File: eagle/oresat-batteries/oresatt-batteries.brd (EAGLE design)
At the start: 160 x 100 mm, 4 parts

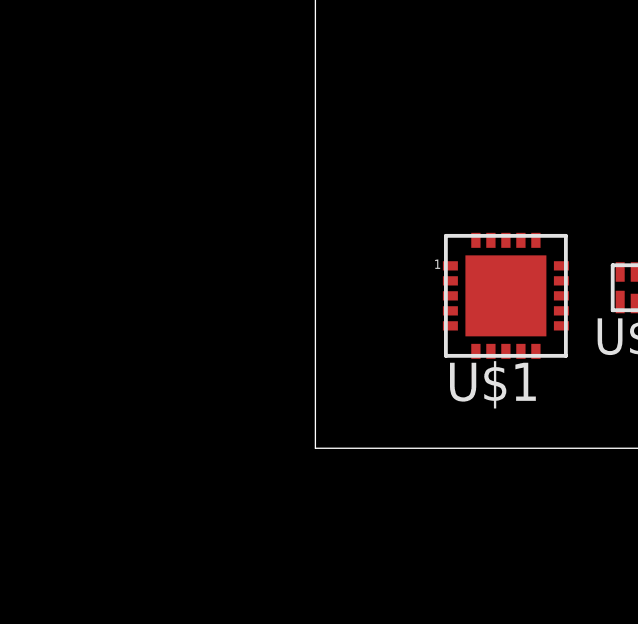
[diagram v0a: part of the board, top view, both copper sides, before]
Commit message: Added crystal, CAN transciever
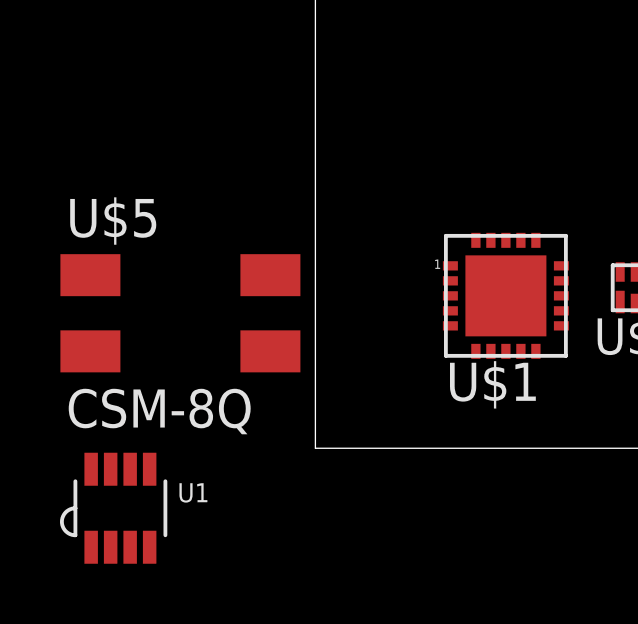
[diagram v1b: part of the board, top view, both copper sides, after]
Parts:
- added U$5: CSM-8Q, oresat-batteries:4-SMD
- added U1: TCAN330, oresat-batteries:SOT23-8_TI-DCN
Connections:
- new net GND: U1.2
- new net VCC: U1.3
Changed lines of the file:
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@@
 <element name="U$3" library="oresat-batteries" package="WDFN8_3X4" value="LC709203F" x="15.24" y="5.08"/>
 <element name="U$4" library="oresat-batteries" package="UFQFPN-28" value="STM32F042G" x="21" y="11"/>
+<element name="U$5" library="oresat-batteries" package="4-SMD" value="CSM-8Q" x="-4.5" y="4.5"/>
+<element name="U1" library="oresat-batteries" package="SOT23-8_TI-DCN" value="TCAN330" x="-6.5" y="-2"/>
 </elements>
 <signals>
@@
 <contactref element="U$4" pad="18"/>
 </signal>
+<signal name="GND">
+<contactref element="U1" pad="2"/>
+</signal>
+<signal name="VCC">
+<contactref element="U1" pad="3"/>
+</signal>
 </signals>

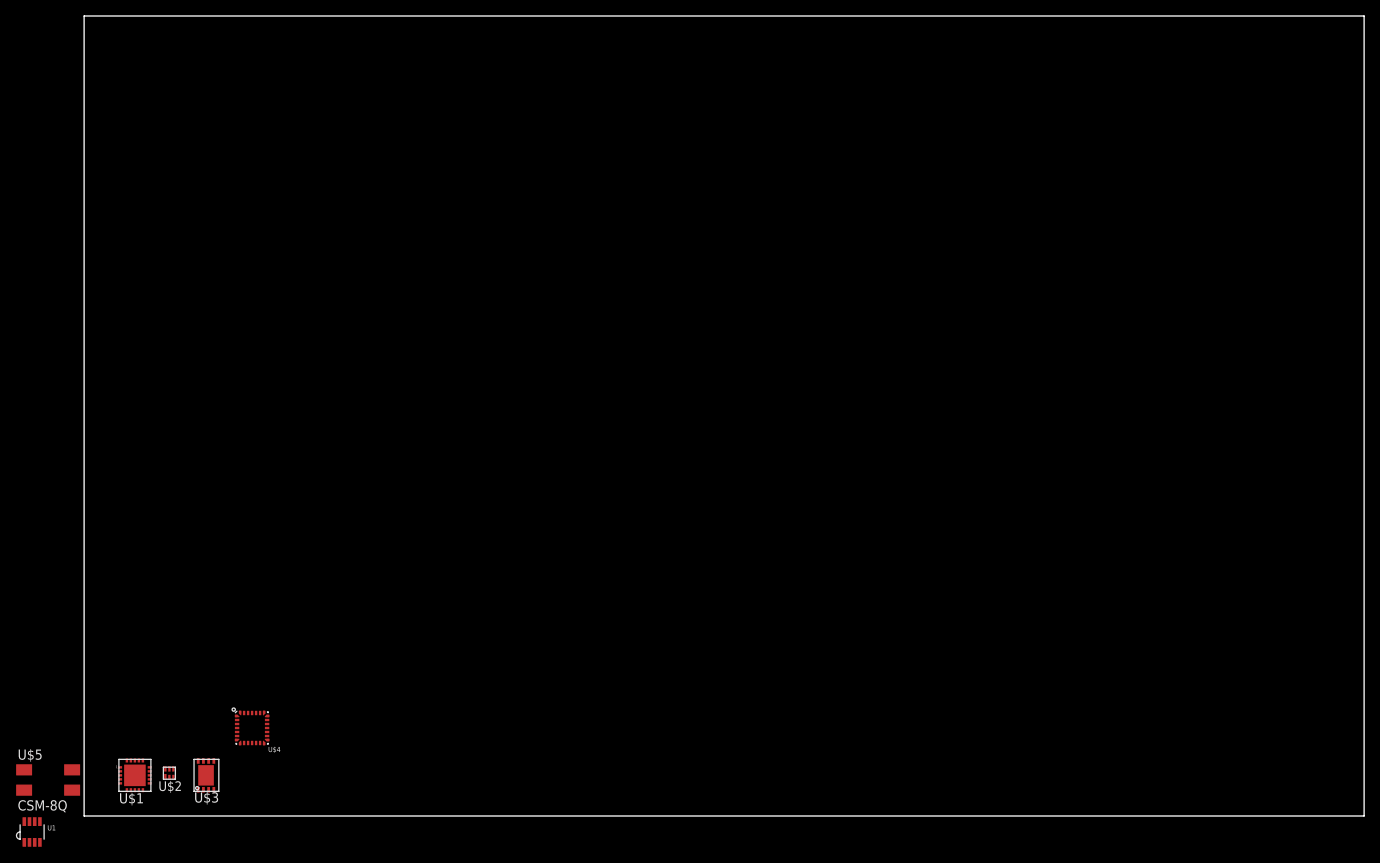
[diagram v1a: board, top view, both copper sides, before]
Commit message: Changed board to real max dimensions.  Added 40pin connector
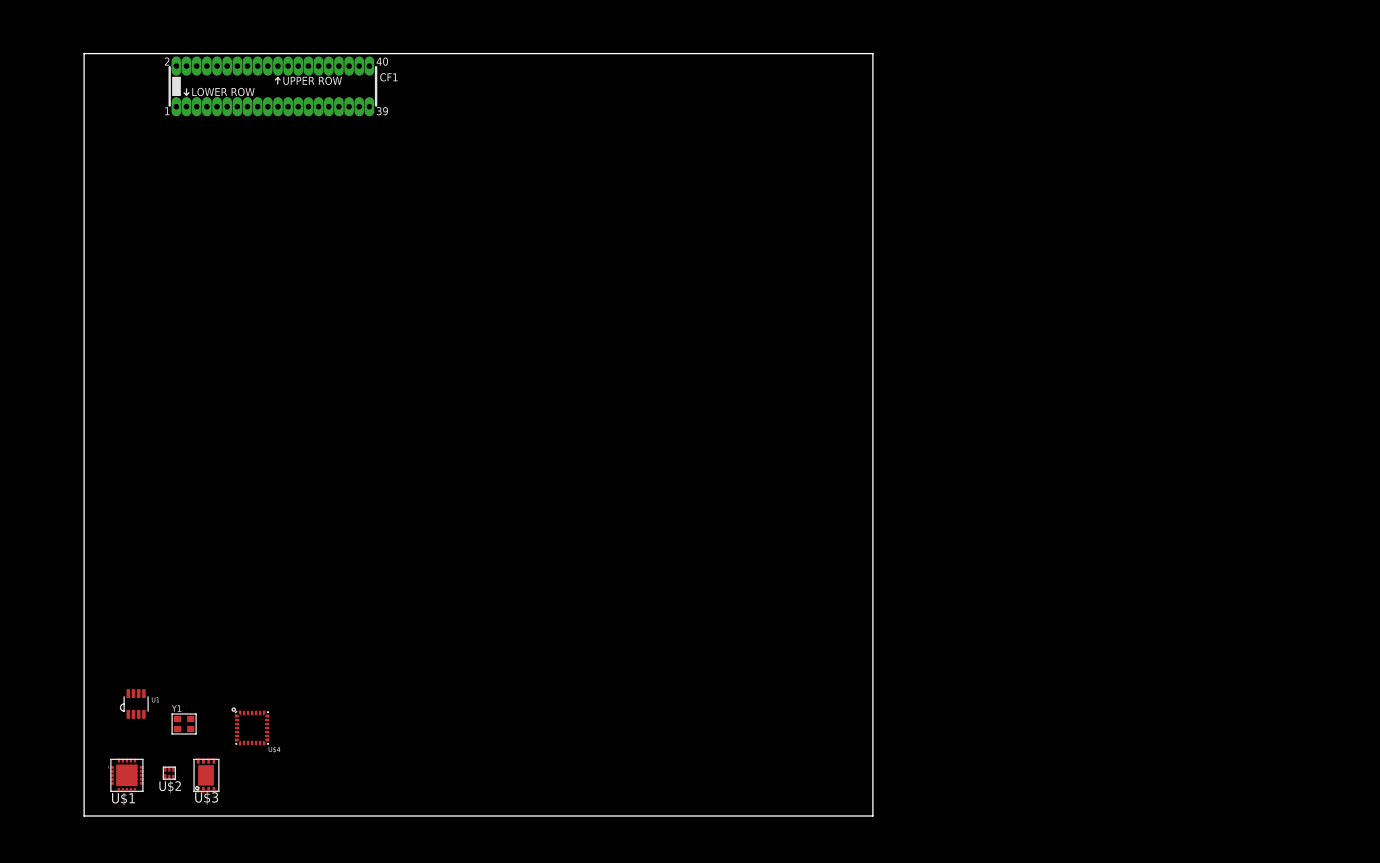
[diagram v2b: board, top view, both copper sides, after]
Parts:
- removed U$5: CSM-8Q, oresat-batteries:4-SMD
- added CF1: ORESAT-CONNECTOR-40PIN, low-gain-radio:HARWIN-ARCHER-M50-3202045
- added Y1: (no value), low-gain-radio:CRYSTAL_2.5X2
- moved U1 20.6 mm to (6.50, 14.0)
- moved U$1 1.00 mm to (5.35, 5.08)
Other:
- board size 160 x 100 mm -> 98.6 x 95.3 mm
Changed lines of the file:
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@@
 <setting verticaltext="up"/>
 </settings>
-<grid distance="0.5" unitdist="mm" unit="mm" style="lines" multiple="1" display="yes" altdistance="0.025" altunitdist="inch" altunit="inch"/>
+<grid distance="0.1" unitdist="mm" unit="mm" style="lines" multiple="1" display="yes" altdistance="0.025" altunitdist="inch" altunit="inch"/>
 <layers>
 <layer number="1" name="Top" color="4" fill="1" visible="yes" active="yes"/>
@@
 <layer number="48" name="Document" color="7" fill="1" visible="yes" active="yes"/>
 <layer number="49" name="Reference" color="7" fill="1" visible="yes" active="yes"/>
+<layer number="50" name="dxf" color="7" fill="1" visible="yes" active="yes"/>
 <layer number="51" name="tDocu" color="7" fill="1" visible="yes" active="yes"/>
 <layer number="52" name="bDocu" color="7" fill="1" visible="yes" active="yes"/>
+<layer number="53" name="tGND_GNDA" color="7" fill="1" visible="yes" active="yes"/>
+<layer number="54" name="bGND_GNDA" color="7" fill="1" visible="yes" active="yes"/>
+<layer number="56" name="wert" color="7" fill="1" visible="yes" active="yes"/>
+<layer number="57" name="tCAD" color="7" fill="1" visible="yes" active="yes"/>
+<layer number="58" name="b3D" color="7" fill="1" visible="yes" active="yes"/>
+<layer number="59" name="Invisible" color="7" fill="1" visible="yes" active="yes"/>
+<layer number="61" name="stand" color="7" fill="1" visible="yes" active="yes"/>
 <layer number="90" name="Modules" color="5" fill="1" visible="no" active="no"/>
 <layer number="91" name="Nets" color="2" fill="1" visible="no" active="no"/>
@@
 <layer number="97" name="Info" color="7" fill="1" visible="no" active="no"/>
 <layer number="98" name="Guide" color="6" fill="1" visible="no" active="no"/>
+<layer number="99" name="SpiceOrder" color="7" fill="1" visible="no" active="no"/>
+<layer number="100" name="TODO" color="7" fill="1" visible="yes" active="yes"/>
+<layer number="101" name="Hidden" color="7" fill="1" visible="yes" active="yes"/>
+<layer number="102" name="Changes" color="7" fill="1" visible="yes" active="yes"/>
+<layer number="103" name="tMap" color="7" fill="1" visible="yes" active="yes"/>
+<layer number="104" name="Name" color="7" fill="1" visible="yes" active="yes"/>
+<layer number="105" name="Beschreib" color="7" fill="1" visible="yes" active="yes"/>
+<layer number="106" name="BGA-Top" color="7" fill="1" visible="yes" active="yes"/>
+<layer number="107" name="BD-Top" color="7" fill="1" visible="yes" active="yes"/>
+<layer number="108" name="tplace-old" color="7" fill="1" visible="yes" active="yes"/>
+<layer number="109" name="ref-old" color="7" fill="1" visible="yes" active="yes"/>
+<layer number="110" name="fp0" color="7" fill="1" visible="yes" active="yes"/>
+<layer number="111" name="LPC17xx" color="7" fill="1" visible="yes" active="yes"/>
+<layer number="112" name="tSilk" color="7" fill="1" visible="yes" active="yes"/>
+<layer number="113" name="ReferenceLS" color="7" fill="1" visible="yes" active="yes"/>
+<layer number="114" name="secv1" color="7" fill="1" visible="yes" active="yes"/>
+<layer number="115" name="secv12" color="7" fill="1" visible="yes" active="yes"/>
+<layer number="116" name="Patch_BOT" color="7" fill="1" visible="yes" active="yes"/>
+<layer number="117" name="secv21" color="7" fill="1" visible="yes" active="yes"/>
+<layer number="118" name="Rect_Pads" color="7" fill="1" visible="yes" active="yes"/>
+<layer number="121" name="_tsilk" color="7" fill="1" visible="yes" active="yes"/>
+<layer number="122" name="_bsilk" color="7" fill="1" visible="yes" active="yes"/>
+<layer number="123" name="tTestmark" color="7" fill="1" visible="yes" active="yes"/>
+<layer number="124" name="bTestmark" color="7" fill="1" visible="yes" active="yes"/>
+<layer number="125" name="_tNames" color="7" fill="1" visible="yes" active="yes"/>
+<layer number="126" name="_bNames" color="7" fill="1" visible="yes" active="yes"/>
+<layer number="127" name="_tValues" color="7" fill="1" visible="yes" active="yes"/>
+<layer number="128" name="_bValues" color="7" fill="1" visible="yes" active="yes"/>
+<layer number="130" name="bLogo" color="7" fill="1" visible="yes" active="yes"/>
+<layer number="131" name="tAdjust" color="7" fill="1" visible="yes" active="yes"/>
+<layer number="132" name="bAdjust" color="7" fill="1" visible="yes" active="yes"/>
+<layer number="144" name="Drill_legend" color="7" fill="1" visible="yes" active="yes"/>
+<layer number="150" name="Notes" color="7" fill="1" visible="yes" active="yes"/>
+<layer number="151" name="HeatSink" color="7" fill="1" visible="yes" active="yes"/>
+<layer number="152" name="_bDocu" color="7" fill="1" visible="yes" active="yes"/>
+<layer number="153" name="FabDoc1" color="7" fill="1" visible="yes" active="yes"/>
+<layer number="154" name="FabDoc2" color="7" fill="1" visible="yes" active="yes"/>
+<layer number="155" name="FabDoc3" color="7" fill="1" visible="yes" active="yes"/>
+<layer number="199" name="Contour" color="7" fill="1" visible="yes" active="yes"/>
+<layer number="200" name="200bmp" color="7" fill="1" visible="yes" active="yes"/>
+<layer number="201" name="201bmp" color="7" fill="1" visible="yes" active="yes"/>
+<layer number="202" name="202bmp" color="7" fill="1" visible="yes" active="yes"/>
+<layer number="203" name="203bmp" color="7" fill="1" visible="yes" active="yes"/>
+<layer number="204" name="204bmp" color="7" fill="1" visible="yes" active="yes"/>
+<layer number="205" name="205bmp" color="7" fill="1" visible="yes" active="yes"/>
+<layer number="206" name="206bmp" color="7" fill="1" visible="yes" active="yes"/>
+<layer number="207" name="207bmp" color="7" fill="1" visible="yes" active="yes"/>
+<layer number="208" name="208bmp" color="7" fill="1" visible="yes" active="yes"/>
+<layer number="209" name="209bmp" color="7" fill="1" visible="yes" active="yes"/>
+<layer number="210" name="210bmp" color="7" fill="1" visible="yes" active="yes"/>
+<layer number="211" name="211bmp" color="7" fill="1" visible="yes" active="yes"/>
+<layer number="212" name="212bmp" color="7" fill="1" visible="yes" active="yes"/>
+<layer number="213" name="213bmp" color="7" fill="1" visible="yes" active="yes"/>
+<layer number="214" name="214bmp" color="7" fill="1" visible="yes" active="yes"/>
+<layer number="215" name="215bmp" color="7" fill="1" visible="yes" active="yes"/>
+<layer number="216" name="216bmp" color="7" fill="1" visible="yes" active="yes"/>
+<layer number="217" name="217bmp" color="7" fill="1" visible="yes" active="yes"/>
+<layer number="218" name="218bmp" color="7" fill="1" visible="yes" active="yes"/>
+<layer number="219" name="219bmp" color="7" fill="1" visible="yes" active="yes"/>
+<layer number="220" name="220bmp" color="7" fill="1" visible="yes" active="yes"/>
+<layer number="221" name="221bmp" color="7" fill="1" visible="yes" active="yes"/>
+<layer number="222" name="222bmp" color="7" fill="1" visible="yes" active="yes"/>
+<layer number="223" name="223bmp" color="7" fill="1" visible="yes" active="yes"/>
+<layer number="224" name="224bmp" color="7" fill="1" visible="yes" active="yes"/>
+<layer number="225" name="225bmp" color="7" fill="1" visible="yes" active="yes"/>
+<layer number="226" name="226bmp" color="7" fill="1" visible="yes" active="yes"/>
+<layer number="227" name="227bmp" color="7" fill="1" visible="yes" active="yes"/>
+<layer number="228" name="228bmp" color="7" fill="1" visible="yes" active="yes"/>
+<layer number="231" name="Eagle3D_PG1" color="7" fill="1" visible="yes" active="yes"/>
+<layer number="232" name="Eagle3D_PG2" color="7" fill="1" visible="yes" active="yes"/>
+<layer number="233" name="Eagle3D_PG3" color="7" fill="1" visible="yes" active="yes"/>
+<layer number="248" name="Housing" color="7" fill="1" visible="yes" active="yes"/>
+<layer number="249" name="Edge" color="7" fill="1" visible="yes" active="yes"/>
+<layer number="250" name="Descript" color="7" fill="1" visible="yes" active="yes"/>
+<layer number="251" name="SMDround" color="7" fill="1" visible="yes" active="yes"/>
+<layer number="254" name="cooling" color="7" fill="1" visible="yes" active="yes"/>
 </layers>
 <board>
 <plain>
-<wire x1="0" y1="0" x2="160" y2="0" width="0" layer="20"/>
-<wire x1="160" y1="0" x2="160" y2="100" width="0" layer="20"/>
-<wire x1="160" y1="100" x2="0" y2="100" width="0" layer="20"/>
-<wire x1="0" y1="100" x2="0" y2="0" width="0" layer="20"/>
+<wire x1="0" y1="0" x2="98.6" y2="0" width="0" layer="20"/>
+<wire x1="98.6" y1="0" x2="98.6" y2="95.3" width="0" layer="20"/>
+<wire x1="98.6" y1="95.3" x2="0" y2="95.3" width="0" layer="20"/>
+<wire x1="0" y1="95.3" x2="0" y2="0" width="0" layer="20"/>
 </plain>
 <attributes>
@@
 </autorouter>
 <elements>
-<element name="U$1" library="oresat-batteries" package="20_4X4_VVTQ" value="ADP5063" x="6.35" y="5.08"/>
+<element name="U$1" library="oresat-batteries" package="20_4X4_VVTQ" value="ADP5063" x="5.35" y="5.08"/>
 <element name="U$2" library="oresat-batteries" package="PSOP6" value="BQ2970" x="10.66" y="5.35"/>
 <element name="U$3" library="oresat-batteries" package="WDFN8_3X4" value="LC709203F" x="15.24" y="5.08"/>
 <element name="U$4" library="oresat-batteries" package="UFQFPN-28" value="STM32F042G" x="21" y="11"/>
-<element name="U$5" library="oresat-batteries" package="4-SMD" value="CSM-8Q" x="-4.5" y="4.5"/>
-<element name="U1" library="oresat-batteries" package="SOT23-8_TI-DCN" value="TCAN330" x="-6.5" y="-2"/>
+<element name="U1" library="oresat-batteries" package="SOT23-8_TI-DCN" value="TCAN330" x="6.5" y="14"/>
+<element name="Y1" library="low-gain-radio" package="CRYSTAL_2.5X2" value="" x="12.5" y="11.5"/>
+<element name="CF1" library="low-gain-radio" package="HARWIN-ARCHER-M50-3202045" value="ORESAT-CONNECTOR-40PIN" x="23.6" y="91.2"/>
 </elements>
 <signals>

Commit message: Removed locks!
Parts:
- removed CF1: ORESAT-CONNECTOR-40PIN, low-gain-radio:HARWIN-ARCHER-M50-3202045
- moved Y1 23.7 mm to (29.5, 28.0)
- moved U1 22.4 mm to (24.0, 28.0)
- moved U$1 1.00 mm to (6.35, 5.08)
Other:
- board size 98.6 x 95.3 mm -> 160 x 100 mm
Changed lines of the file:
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@@
 <setting verticaltext="up"/>
 </settings>
-<grid distance="0.1" unitdist="mm" unit="mm" style="lines" multiple="1" display="yes" altdistance="0.025" altunitdist="inch" altunit="inch"/>
+<grid distance="0.5" unitdist="mm" unit="mm" style="lines" multiple="1" display="yes" altdistance="0.025" altunitdist="inch" altunit="inch"/>
 <layers>
 <layer number="1" name="Top" color="4" fill="1" visible="yes" active="yes"/>
@@
 <board>
 <plain>
-<wire x1="0" y1="0" x2="98.6" y2="0" width="0" layer="20"/>
-<wire x1="98.6" y1="0" x2="98.6" y2="95.3" width="0" layer="20"/>
-<wire x1="98.6" y1="95.3" x2="0" y2="95.3" width="0" layer="20"/>
-<wire x1="0" y1="95.3" x2="0" y2="0" width="0" layer="20"/>
+<wire x1="0" y1="0" x2="160" y2="0" width="0" layer="20"/>
+<wire x1="160" y1="0" x2="160" y2="100" width="0" layer="20"/>
+<wire x1="160" y1="100" x2="0" y2="100" width="0" layer="20"/>
+<wire x1="0" y1="100" x2="0" y2="0" width="0" layer="20"/>
 </plain>
 <attributes>
@@
 </autorouter>
 <elements>
-<element name="U$1" library="oresat-batteries" package="20_4X4_VVTQ" value="ADP5063" x="5.35" y="5.08"/>
+<element name="U$1" library="oresat-batteries" package="20_4X4_VVTQ" value="ADP5063" x="6.35" y="5.08"/>
 <element name="U$2" library="oresat-batteries" package="PSOP6" value="BQ2970" x="10.66" y="5.35"/>
 <element name="U$3" library="oresat-batteries" package="WDFN8_3X4" value="LC709203F" x="15.24" y="5.08"/>
 <element name="U$4" library="oresat-batteries" package="UFQFPN-28" value="STM32F042G" x="21" y="11"/>
-<element name="U1" library="oresat-batteries" package="SOT23-8_TI-DCN" value="TCAN330" x="6.5" y="14"/>
-<element name="Y1" library="low-gain-radio" package="CRYSTAL_2.5X2" value="" x="12.5" y="11.5"/>
-<element name="CF1" library="low-gain-radio" package="HARWIN-ARCHER-M50-3202045" value="ORESAT-CONNECTOR-40PIN" x="23.6" y="91.2"/>
+<element name="U1" library="oresat-batteries" package="SOT23-8_TI-DCN" value="TCAN330" x="24" y="28"/>
+<element name="Y1" library="low-gain-radio" package="CRYSTAL_2.5X2" value="" x="29.5" y="28"/>
 </elements>
 <signals>
